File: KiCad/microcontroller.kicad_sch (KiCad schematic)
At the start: 11 parts, among them J1 Debugger, SW1 Reset switch, U1 STM32F051C6Tx, U7 24LC256

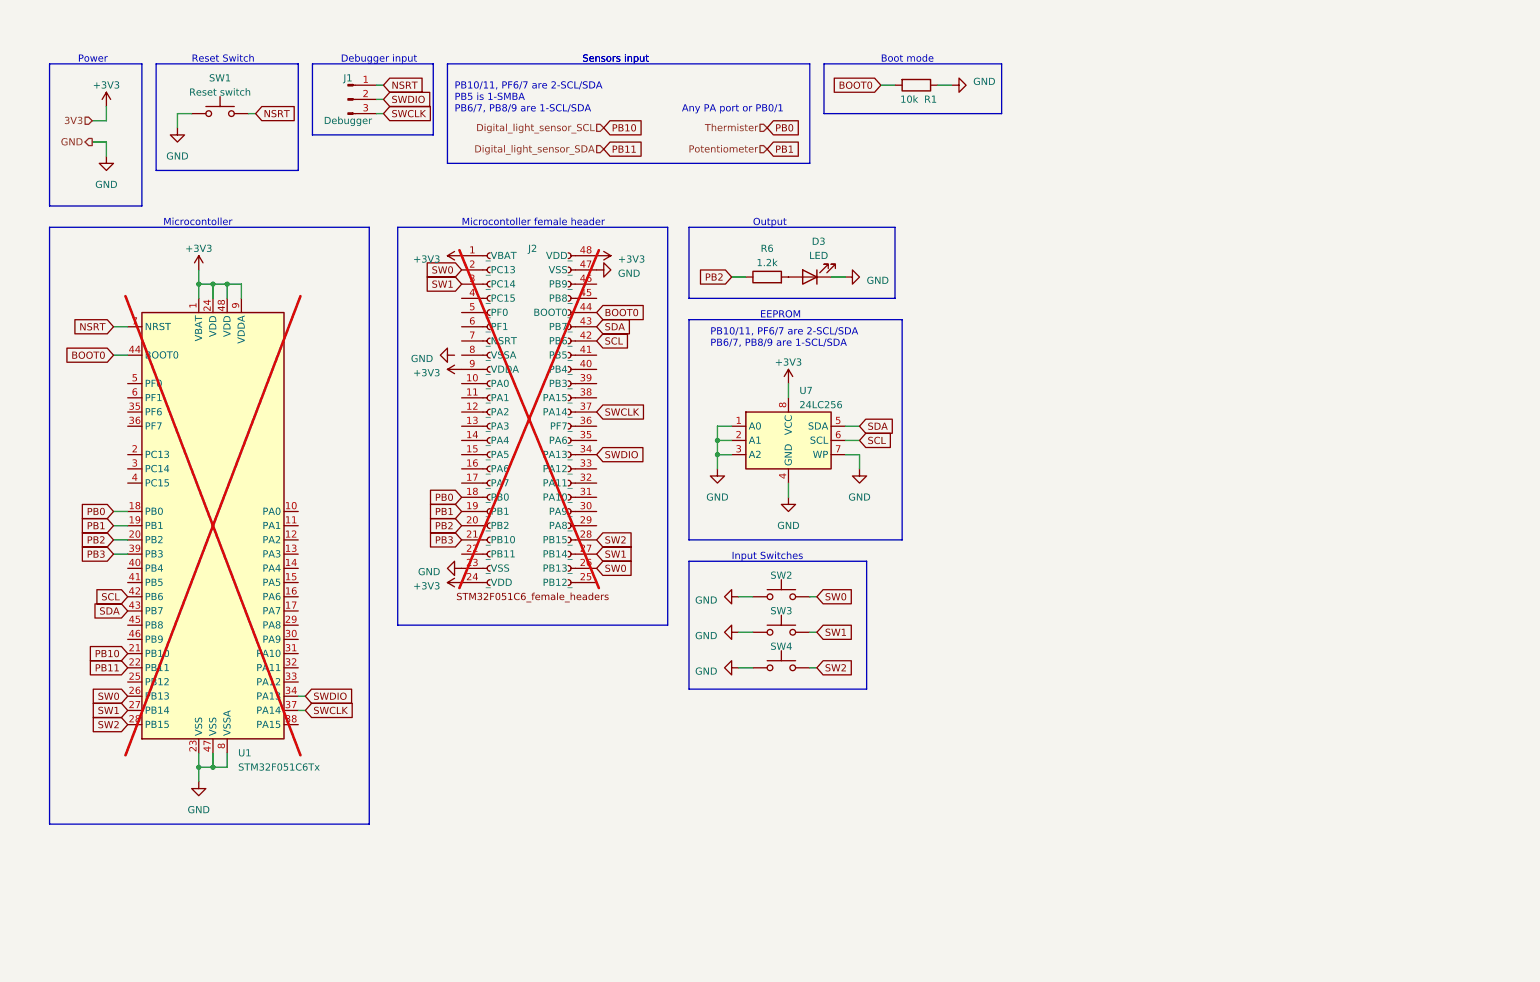
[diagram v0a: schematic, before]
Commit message: added heirachals and connected subsheets
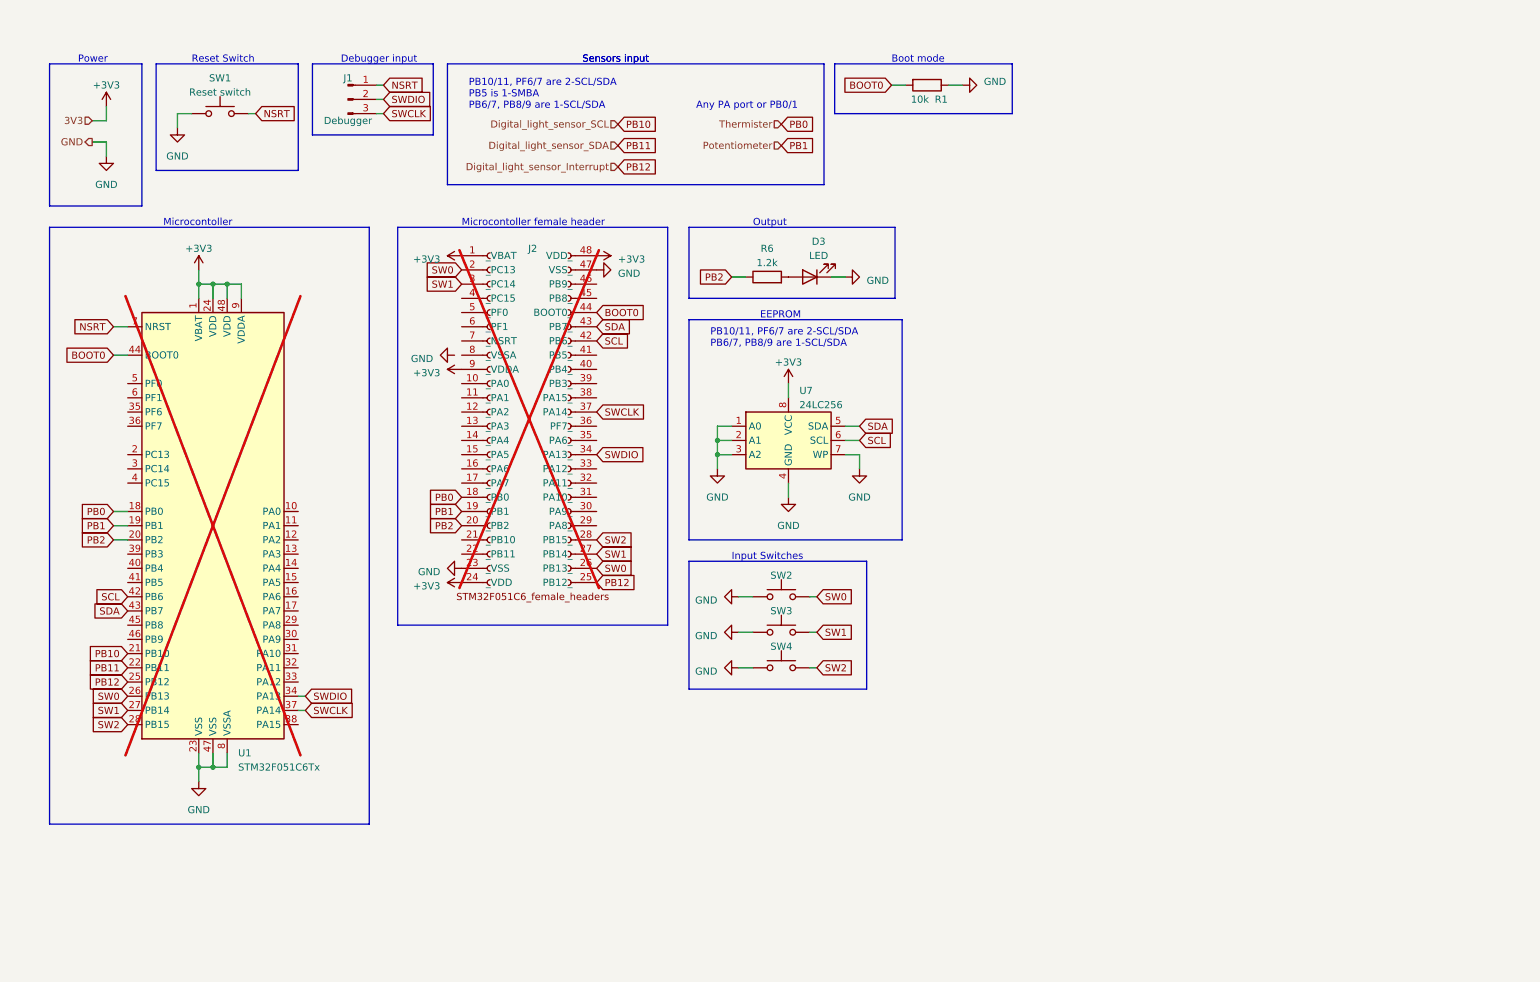
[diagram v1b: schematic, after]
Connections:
- net PB12: now reaches J2.25 (PB12_)
- net PB12: now also U1.25 (PB12)
- net PB3: no longer names the net of J2.21 (_PB10)
- net PB3: no longer U1.39 (PB3)
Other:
- moved on the sheet: R1
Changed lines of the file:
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@@
-    (stroke (width 0) (type default))
-  )
-  (wire (pts (xy 30.48 109.22) (xy 33.02 109.22))
     (stroke (width 0) (type default))
   )
@@
     (stroke (width 0) (type default))
   )
-  (wire (pts (xy 180.34 25.4) (xy 177.8 25.4))
+  (wire (pts (xy 182.245 25.4) (xy 179.705 25.4))
     (stroke (width 0) (type default))
   )
@@
     (stroke (width 0) (type default))
   )
-  (wire (pts (xy 167.64 25.4) (xy 170.18 25.4))
+  (wire (pts (xy 169.545 25.4) (xy 172.085 25.4))
     (stroke (width 0) (type default))
   )
@@
     (stroke (width 0) (type default))
   )
-  (rectangle (start 157.48 21.59) (end 189.23 30.48)
+  (rectangle (start 159.385 21.59) (end 191.135 30.48)
     (stroke (width 0) (type default))
     (fill (type none))
@@
     (fill (type none))
   )
-  (rectangle (start 90.17 21.59) (end 154.94 39.37)
+  (rectangle (start 90.17 21.59) (end 157.48 43.18)
     (stroke (width 0) (type default))
     (fill (type none))
@@
     (effects (font (size 1.27 1.27)) (justify left bottom))
   )
-  (text "Any PA port or PB0/1" (at 132.08 30.48 0)
+  (text "Any PA port or PB0/1" (at 134.62 29.845 0)
     (effects (font (size 1.27 1.27)) (justify left bottom))
   )
@@
     (effects (font (size 1.27 1.27)) (justify left bottom))
   )
-  (text "Boot mode" (at 167.64 21.59 0)
+  (text "Boot mode" (at 169.545 21.59 0)
     (effects (font (size 1.27 1.27)) (justify left bottom))
   )
@@
   )
   (text "PB10/11, PF6/7 are 2-SCL/SDA\nPB5 is 1-SMBA\nPB6/7, PB8/9 are 1-SCL/SDA"
-    (at 91.44 30.48 0)
-    (effects (font (size 1.27 1.27)) (justify left bottom))
-  )
-  (global_label "PB3" (shape input) (at 30.48 109.22 180) (fields_autoplaced)
-    (effects (font (size 1.27 1.27)) (justify right))
-    (property "Intersheetrefs" "${INTERSHEET_REFS}" (at 23.8247 109.22 0)
-      (effects (font (size 1.27 1.27)) (justify right) hide)
-    )
-  )
-  (global_label "PB1" (shape input) (at 147.32 36.83 0) (fields_autoplaced)
-    (effects (font (size 1.27 1.27)) (justify left))
-    (property "Intersheetrefs" "${INTERSHEET_REFS}" (at 153.9753 36.83 0)
+    (at 93.98 29.845 0)
+    (effects (font (size 1.27 1.27)) (justify left bottom))
+  )
+  (global_label "PB1" (shape input) (at 149.86 36.195 0) (fields_autoplaced)
+    (effects (font (size 1.27 1.27)) (justify left))
+    (property "Intersheetrefs" "${INTERSHEET_REFS}" (at 156.5153 36.195 0)
       (effects (font (size 1.27 1.27)) (justify left) hide)
     )
@@
     )
   )
+  (global_label "PB12" (shape input) (at 33.02 132.08 180) (fields_autoplaced)
+    (effects (font (size 1.27 1.27)) (justify right))
+    (property "Intersheetrefs" "${INTERSHEET_REFS}" (at 25.1552 132.08 0)
+      (effects (font (size 1.27 1.27)) (justify right) hide)
+    )
+  )
   (global_label "PB0" (shape input) (at 30.48 101.6 180) (fields_autoplaced)
     (effects (font (size 1.27 1.27)) (justify right))
@@
     )
   )
-  (global_label "PB10" (shape input) (at 118.11 33.02 0) (fields_autoplaced)
-    (effects (font (size 1.27 1.27)) (justify left))
-    (property "Intersheetrefs" "${INTERSHEET_REFS}" (at 125.9748 33.02 0)
+  (global_label "PB10" (shape input) (at 120.65 32.385 0) (fields_autoplaced)
+    (effects (font (size 1.27 1.27)) (justify left))
+    (property "Intersheetrefs" "${INTERSHEET_REFS}" (at 128.5148 32.385 0)
       (effects (font (size 1.27 1.27)) (justify left) hide)
     )
@@
     )
   )
-  (global_label "PB11" (shape input) (at 118.11 36.83 0) (fields_autoplaced)
-    (effects (font (size 1.27 1.27)) (justify left))
-    (property "Intersheetrefs" "${INTERSHEET_REFS}" (at 125.9748 36.83 0)
+  (global_label "PB11" (shape input) (at 120.65 36.195 0) (fields_autoplaced)
+    (effects (font (size 1.27 1.27)) (justify left))
+    (property "Intersheetrefs" "${INTERSHEET_REFS}" (at 128.5148 36.195 0)
       (effects (font (size 1.27 1.27)) (justify left) hide)
     )
@@
     )
   )
-  (global_label "PB0" (shape input) (at 147.32 33.02 0) (fields_autoplaced)
-    (effects (font (size 1.27 1.27)) (justify left))
-    (property "Intersheetrefs" "${INTERSHEET_REFS}" (at 153.9753 33.02 0)
-      (effects (font (size 1.27 1.27)) (justify left) hide)
-    )
-  )
-  (global_label "BOOT0" (shape input) (at 167.64 25.4 180) (fields_autoplaced)
-    (effects (font (size 1.27 1.27)) (justify right))
-    (property "Intersheetrefs" "${INTERSHEET_REFS}" (at 158.6261 25.4 0)
+  (global_label "PB0" (shape input) (at 149.86 32.385 0) (fields_autoplaced)
+    (effects (font (size 1.27 1.27)) (justify left))
+    (property "Intersheetrefs" "${INTERSHEET_REFS}" (at 156.5153 32.385 0)
+      (effects (font (size 1.27 1.27)) (justify left) hide)
+    )
+  )
+  (global_label "BOOT0" (shape input) (at 169.545 25.4 180) (fields_autoplaced)
+    (effects (font (size 1.27 1.27)) (justify right))
+    (property "Intersheetrefs" "${INTERSHEET_REFS}" (at 160.5311 25.4 0)
       (effects (font (size 1.27 1.27)) (justify right) hide)
     )
@@
     )
   )
+  (global_label "PB12" (shape input) (at 116.84 114.3 0) (fields_autoplaced)
+    (effects (font (size 1.27 1.27)) (justify left))
+    (property "Intersheetrefs" "${INTERSHEET_REFS}" (at 124.7048 114.3 0)
+      (effects (font (size 1.27 1.27)) (justify left) hide)
+    )
+  )
   (global_label "PB1" (shape input) (at 92.71 101.6 180) (fields_autoplaced)
     (effects (font (size 1.27 1.27)) (justify right))
@@
     )
   )
+  (global_label "PB12" (shape input) (at 120.65 40.005 0) (fields_autoplaced)
+    (effects (font (size 1.27 1.27)) (justify left))
+    (property "Intersheetrefs" "${INTERSHEET_REFS}" (at 128.5148 40.005 0)
+      (effects (font (size 1.27 1.27)) (justify left) hide)
+    )
+  )
   (global_label "SWDIO" (shape input) (at 64.77 134.62 0) (fields_autoplaced)
     (effects (font (size 1.27 1.27)) (justify left))
@@
     )
   )
-  (global_label "PB3" (shape input) (at 92.71 106.68 180) (fields_autoplaced)
-    (effects (font (size 1.27 1.27)) (justify right))
-    (property "Intersheetrefs" "${INTERSHEET_REFS}" (at 86.0547 106.68 0)
-      (effects (font (size 1.27 1.27)) (justify right) hide)
-    )
-  )
   (global_label "NSRT" (shape input) (at 78.74 25.4 0) (fields_autoplaced)
     (effects (font (size 1.27 1.27)) (justify left))
@@
     )
   )
-  (hierarchical_label "Digital_light_sensor_SCL" (shape input) (at 118.11 33.02 180) (fields_autoplaced)
+  (hierarchical_label "Digital_light_sensor_SCL" (shape input) (at 120.65 32.385 180) (fields_autoplaced)
     (effects (font (size 1.27 1.27)) (justify right))
   )
@@
     (effects (font (size 1.27 1.27)) (justify right))
   )
-  (hierarchical_label "Digital_light_sensor_SDA" (shape input) (at 118.11 36.83 180) (fields_autoplaced)
+  (hierarchical_label "Digital_light_sensor_SDA" (shape input) (at 120.65 36.195 180) (fields_autoplaced)
     (effects (font (size 1.27 1.27)) (justify right))
   )
@@
     (effects (font (size 1.27 1.27)) (justify right))
   )
-  (hierarchical_label "Potentiometer" (shape input) (at 147.32 36.83 180) (fields_autoplaced)
-    (effects (font (size 1.27 1.27)) (justify right))
-  )
-  (hierarchical_label "Thermister" (shape input) (at 147.32 33.02 180) (fields_autoplaced)
+  (hierarchical_label "Digital_light_sensor_Interrupt" (shape input) (at 120.65 40.005 180) (fields_autoplaced)
+    (effects (font (size 1.27 1.27)) (justify right))
+  )
+  (hierarchical_label "Potentiometer" (shape input) (at 149.86 36.195 180) (fields_autoplaced)
+    (effects (font (size 1.27 1.27)) (justify right))
+  )
+  (hierarchical_label "Thermister" (shape input) (at 149.86 32.385 180) (fields_autoplaced)
     (effects (font (size 1.27 1.27)) (justify right))
   )
@@
     )
   )
-  (symbol (lib_id "power:GND") (at 180.34 25.4 90) (unit 1)
-    (in_bom yes) (on_board yes) (dnp no) (fields_autoplaced)
-    (property "Reference" "#PWR06" (at 186.69 25.4 0)
-      (effects (font (size 1.27 1.27)) hide)
-    )
-    (property "Value" "GND" (at 184.15 24.765 90)
+  (symbol (lib_id "power:GND") (at 182.245 25.4 90) (unit 1)
+    (in_bom yes) (on_board yes) (dnp no) (fields_autoplaced)
+    (property "Reference" "#PWR06" (at 188.595 25.4 0)
+      (effects (font (size 1.27 1.27)) hide)
+    )
+    (property "Value" "GND" (at 186.055 24.765 90)
       (effects (font (size 1.27 1.27)) (justify right))
     )
-    (property "Footprint" "" (at 180.34 25.4 0)
-      (effects (font (size 1.27 1.27)) hide)
-    )
-    (property "Datasheet" "" (at 180.34 25.4 0)
+    (property "Footprint" "" (at 182.245 25.4 0)
+      (effects (font (size 1.27 1.27)) hide)
+    )
+    (property "Datasheet" "" (at 182.245 25.4 0)
       (effects (font (size 1.27 1.27)) hide)
     )
@@
     )
   )
-  (symbol (lib_id "Device:R") (at 173.99 25.4 270) (unit 1)
+  (symbol (lib_id "Device:R") (at 175.895 25.4 270) (unit 1)
     (in_bom yes) (on_board yes) (dnp no)
-    (property "Reference" "R1" (at 176.53 27.94 90)
-      (effects (font (size 1.27 1.27)))
-    )
-    (property "Value" "10k" (at 172.72 27.94 90)
-      (effects (font (size 1.27 1.27)))
-    )
-    (property "Footprint" "" (at 173.99 23.622 90)
-      (effects (font (size 1.27 1.27)) hide)
-    )
-    (property "Datasheet" "~" (at 173.99 25.4 0)
-      (effects (font (size 1.27 1.27)) hide)
-    )
+    (property "Reference" "R1" (at 178.435 27.94 90)
+      (effects (font (size 1.27 1.27)))
+    )
+    (property "Value" "10k" (at 174.625 27.94 90)
+      (effects (font (size 1.27 1.27)))
+    )
+    (property "Footprint" "" (at 175.895 23.622 90)
+      (effects (font (size 1.27 1.27)) hide)
+    )
+    (property "Datasheet" "~" (at 175.895 25.4 0)
+      (effects (font (size 1.27 1.27)) hide)
+    )
